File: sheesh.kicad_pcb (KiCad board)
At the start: 2 copper layers, 234.7 x 104.6 mm, 142 parts, among them J1 3305-0-15-80-47-27-10-0, J10 3305-0-15-80-47-27-10-0, J11 3305-0-15-80-47-27-10-0, J12 3305-0-15-80-47-27-10-0, J13 3305-0-15-80-47-27-10-0, J14 3305-0-15-80-47-27-10-0, J15 3305-0-15-80-47-27-10-0, J16 3305-0-15-80-47-27-10-0, J17 3305-0-15-80-47-27-10-0, J18 3305-0-15-80-47-27-10-0, J19 3305-0-15-80-47-27-10-0, J2 3305-0-15-80-47-27-10-0, J20 3305-0-15-80-47-27-10-0, J21 3305-0-15-80-47-27-10-0, J22 3305-0-15-80-47-27-10-0, J23 3305-0-15-80-47-27-10-0, J24 3305-0-15-80-47-27-10-0, J25 3305-0-15-80-47-27-10-0, J26 3305-0-15-80-47-27-10-0, J27 3305-0-15-80-47-27-10-0, J28 3305-0-15-80-47-27-10-0, J29 3305-0-15-80-47-27-10-0, J3 3305-0-15-80-47-27-10-0, J30 3305-0-15-80-47-27-10-0, J31 3305-0-15-80-47-27-10-0, J32 3305-0-15-80-47-27-10-0, J33 3305-0-15-80-47-27-10-0, J34 3305-0-15-80-47-27-10-0, J35 3305-0-15-80-47-27-10-0, J36 3305-0-15-80-47-27-10-0, J37 3305-0-15-80-47-27-10-0, J38 3305-0-15-80-47-27-10-0, J39 3305-0-15-80-47-27-10-0, J4 3305-0-15-80-47-27-10-0, J40 3305-0-15-80-47-27-10-0, J41 3305-0-15-80-47-27-10-0, J42 3305-0-15-80-47-27-10-0, J43 3305-0-15-80-47-27-10-0, J44 3305-0-15-80-47-27-10-0, J45 3305-0-15-80-47-27-10-0, J46 3305-0-15-80-47-27-10-0, J47 3305-0-15-80-47-27-10-0, J48 3305-0-15-80-47-27-10-0, J49 3305-0-15-80-47-27-10-0, J5 3305-0-15-80-47-27-10-0, J50 3305-0-15-80-47-27-10-0, J51 3305-0-15-80-47-27-10-0, J52 3305-0-15-80-47-27-10-0, J53 3305-0-15-80-47-27-10-0, J54 3305-0-15-80-47-27-10-0, J55 3305-0-15-80-47-27-10-0, J56 3305-0-15-80-47-27-10-0, J57 MF254V-11-07-0743, J58 MF254V-11-07-0743, J6 3305-0-15-80-47-27-10-0, J61 YZ00615050R-04, J64 MF254V-11-07-0743, J65 MF254V-11-07-0743, J68 YZ00615050R-04, J7 3305-0-15-80-47-27-10-0, J8 3305-0-15-80-47-27-10-0, J9 3305-0-15-80-47-27-10-0, SW1 SW_Push, SW10 SW_Push, SW11 SW_Push, SW12 SW_Push, SW13 SW_Push, SW14 SW_Push, SW15 SW_Push, SW16 SW_Push, SW17 SW_Push, SW18 SW_Push, SW19 SW_Push, SW2 SW_Push, SW20 SW_Push, SW21 SW_Push, SW22 SW_Push, SW23 SW_Push, SW24 SW_Push, SW25 SW_Push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

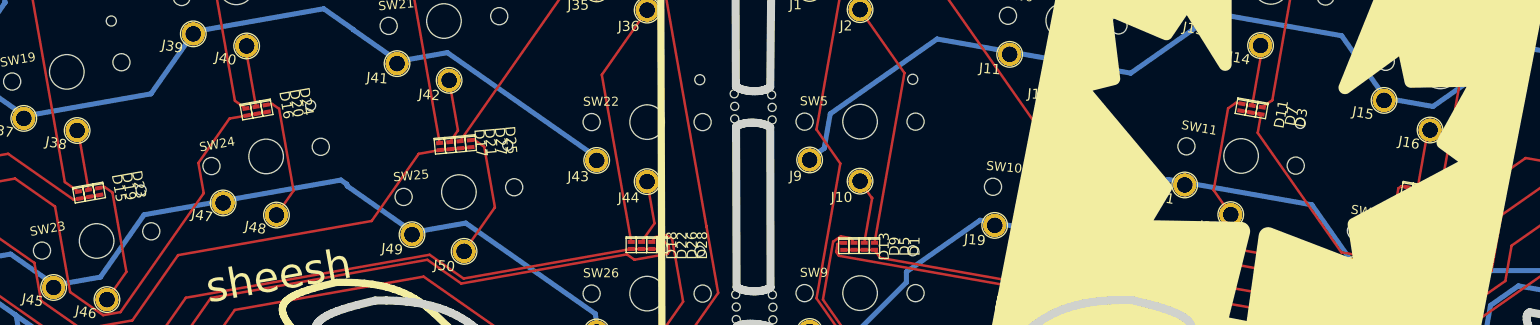
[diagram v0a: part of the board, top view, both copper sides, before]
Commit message: correct diode text and part number
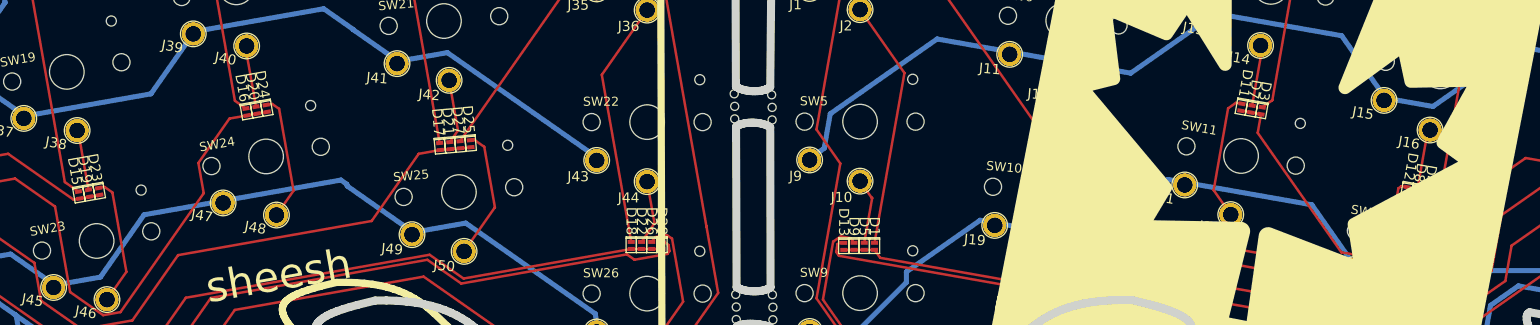
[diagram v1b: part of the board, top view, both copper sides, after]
